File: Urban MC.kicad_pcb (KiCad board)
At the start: 4 copper layers, 166.4 x 125.1 mm, 78 parts, among them J1 Conn_01x02, J2 Conn_01x02, J3 Conn_01x03, J4 Conn_01x02, Q1 IQE022N06LM5CGSCATMA1, Q10 IQE022N06LM5CGSCATMA1, Q11 IQE022N06LM5CGSCATMA1, Q12 IQE022N06LM5CGSCATMA1, Q13 IQE022N06LM5CGSCATMA1, Q14 IQE022N06LM5CGSCATMA1, Q15 IQE022N06LM5CGSCATMA1, Q16 IQE022N06LM5CGSCATMA1, Q17 IQE022N06LM5CGSCATMA1, Q18 IQE022N06LM5CGSCATMA1, Q19 IQE022N06LM5CGSCATMA1, Q2 IQE022N06LM5CGSCATMA1, Q20 IQE022N06LM5CGSCATMA1, Q21 IQE022N06LM5CGSCATMA1, Q22 IQE022N06LM5CGSCATMA1, Q23 IQE022N06LM5CGSCATMA1, Q24 IQE022N06LM5CGSCATMA1, Q3 IQE022N06LM5CGSCATMA1, Q4 IQE022N06LM5CGSCATMA1, Q5 IQE022N06LM5CGSCATMA1, Q6 IQE022N06LM5CGSCATMA1, Q7 IQE022N06LM5CGSCATMA1, Q8 IQE022N06LM5CGSCATMA1, Q9 IQE022N06LM5CGSCATMA1, SW1 CAN_TERM, SW2 SW_Push, U1 MCP2561/2, U2 MCP4725, U3 MCP2515-xSO, Y1 8MHz

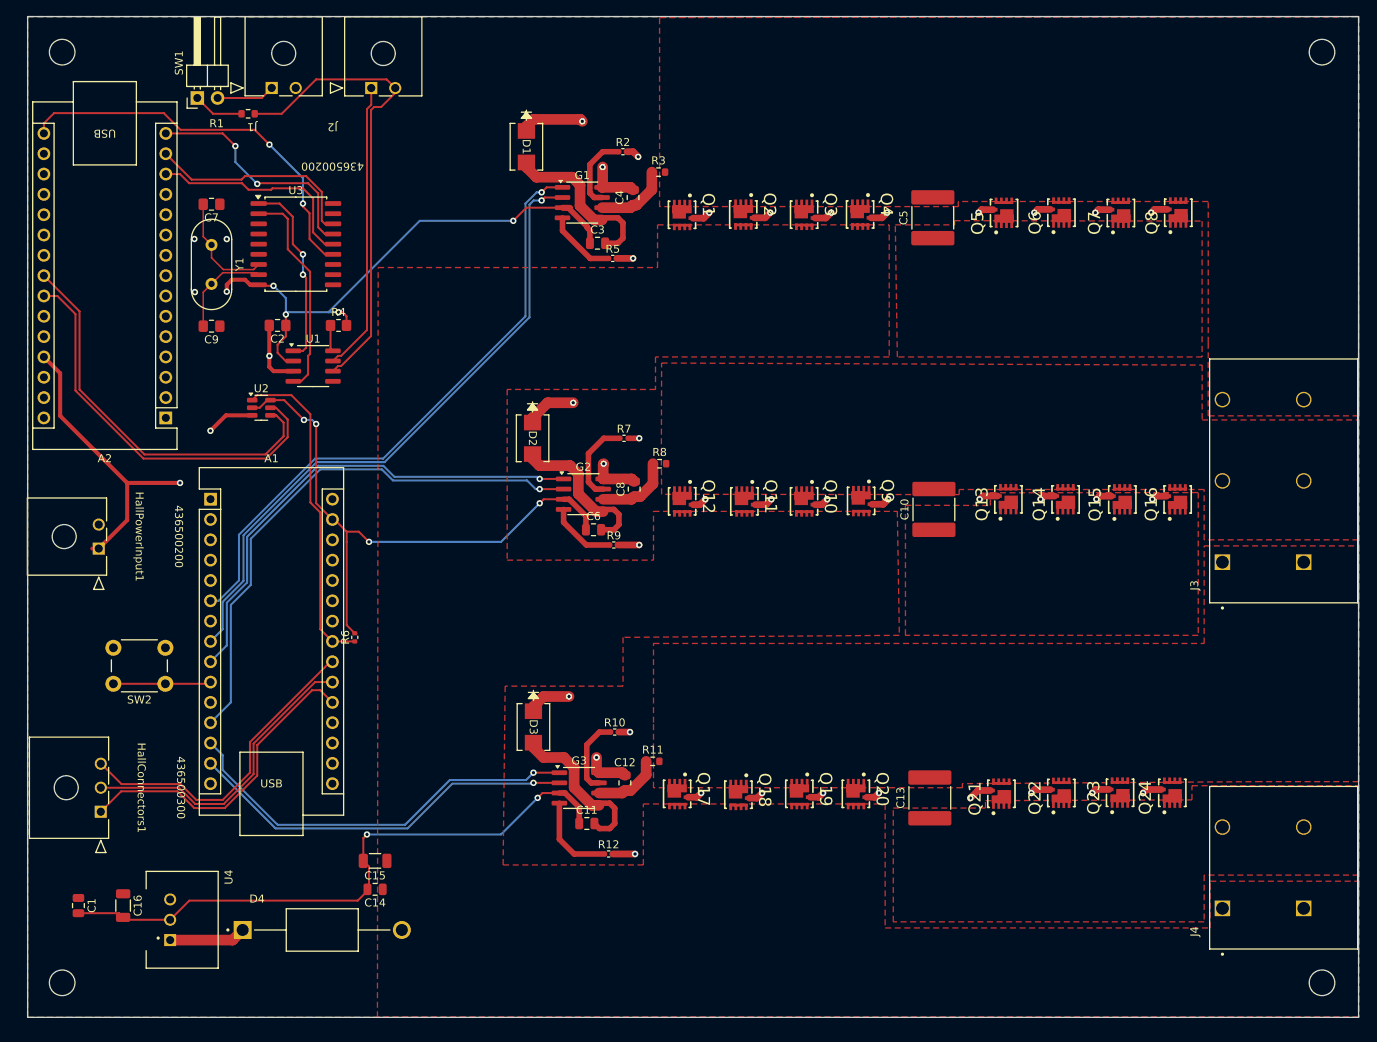
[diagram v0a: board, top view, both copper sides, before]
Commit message: Duplicated filled zones, finished CAN section, organized component labels
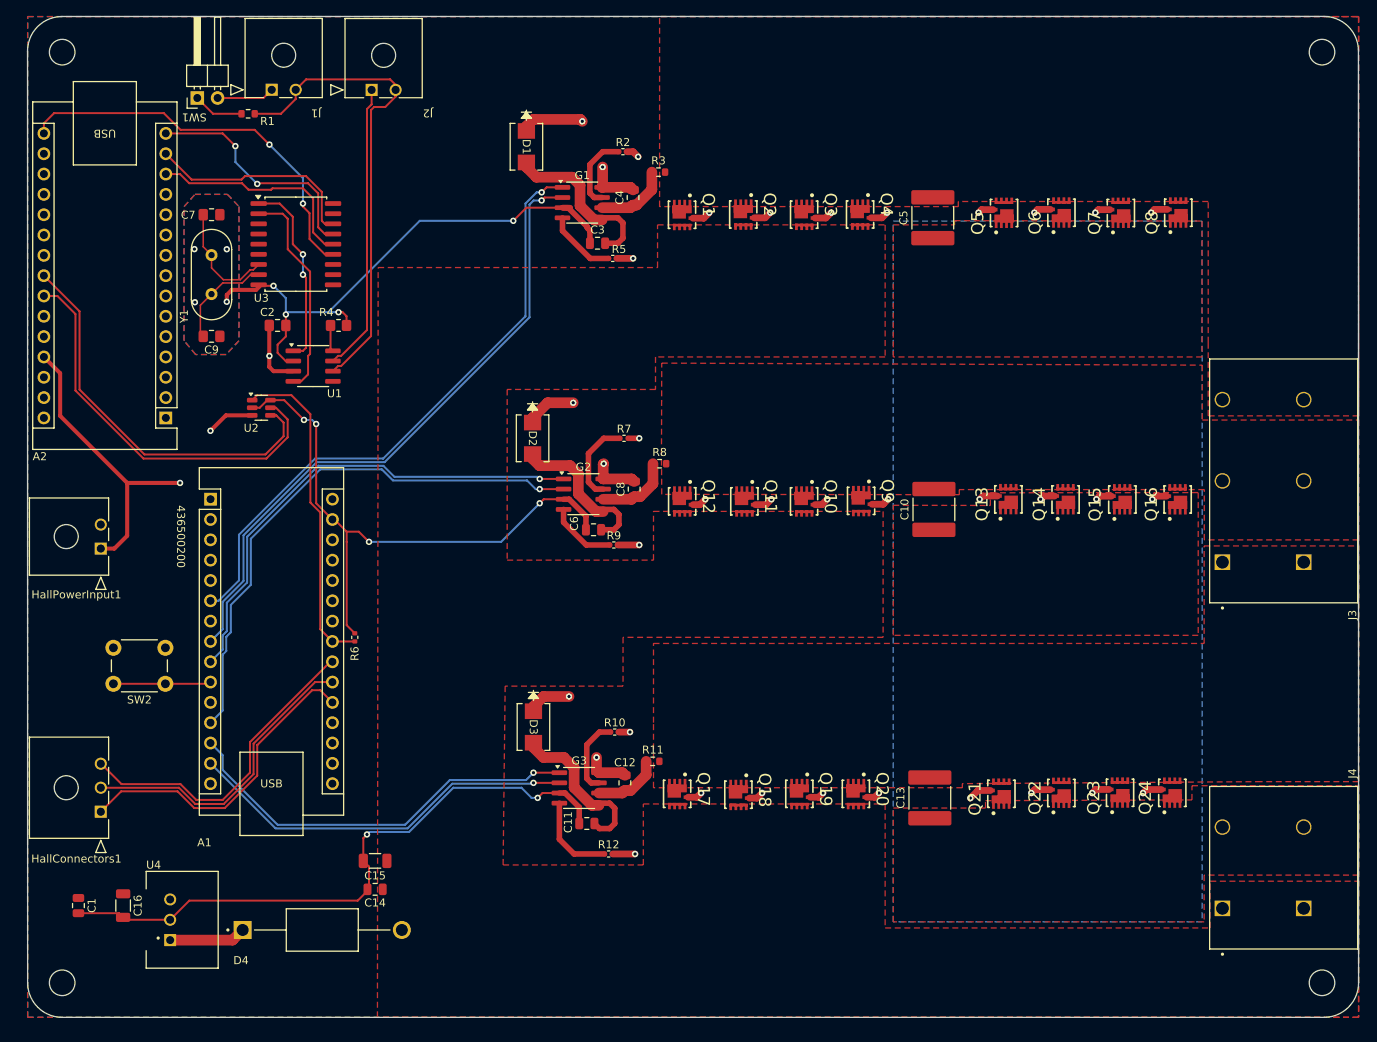
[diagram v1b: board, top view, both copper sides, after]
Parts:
- moved C7 1.31 mm to (115.7, 53.3)
- moved C9 1.27 mm to (115.7, 68.5)
- moved Y1 1.27 mm to (115.7, 58.4)
- moved HallPowerInput1 0.26 mm to (101.9, 95.1)
- moved J2 0.24 mm to (135.7, 37.7)
- moved J1 0.23 mm to (123.2, 37.7)
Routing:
- net /CAN LOW: track 59.2 -> 61.0 mm
- net GND: track 220.3 -> 221.5 mm
- net C-: track 12.3 -> 12.9 mm
- added copper zone on In1.Cu, net +48V
- added copper zone on B.Cu, net GND
- added copper zone on In1.Cu, net Net-(J3-Pin_1)
- added copper zone on In1.Cu, net Net-(J3-Pin_2)
- added copper zone on In1.Cu, net Net-(J3-Pin_3)
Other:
- outline, holes or cut-outs redrawn

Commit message: vias
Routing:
- net Net-(J3-Pin_3): vias 0 -> 61
- net Net-(J3-Pin_2): vias 0 -> 33
- net Net-(J3-Pin_1): vias 0 -> 41
- net GND: vias 14 -> 94
- net +48V: vias 0 -> 180

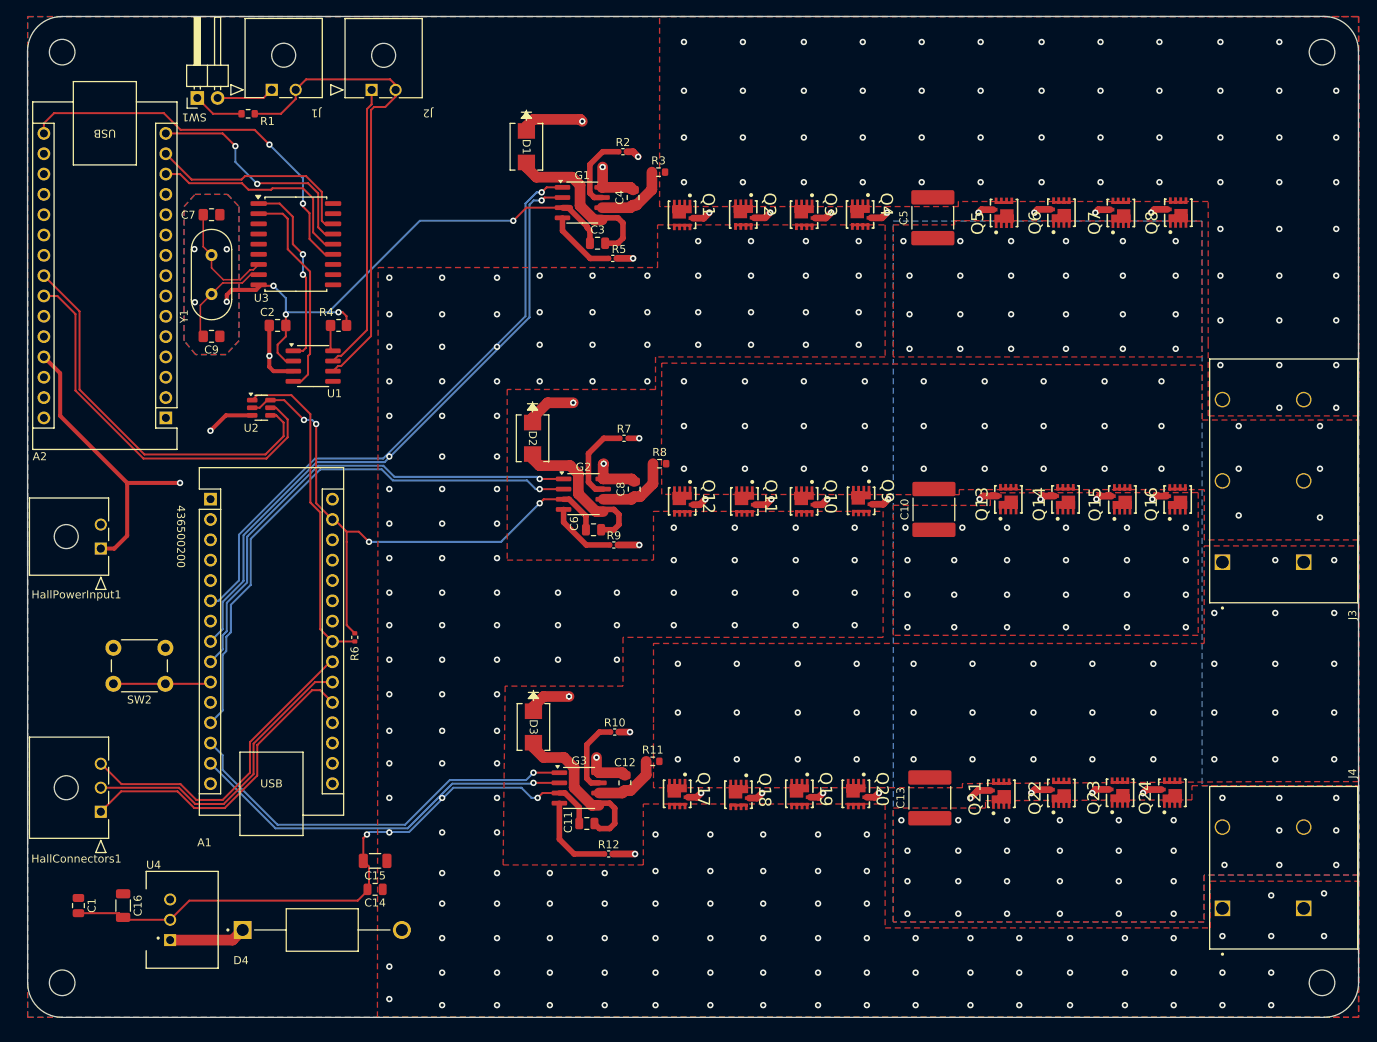
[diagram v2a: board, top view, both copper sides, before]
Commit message: connector labels
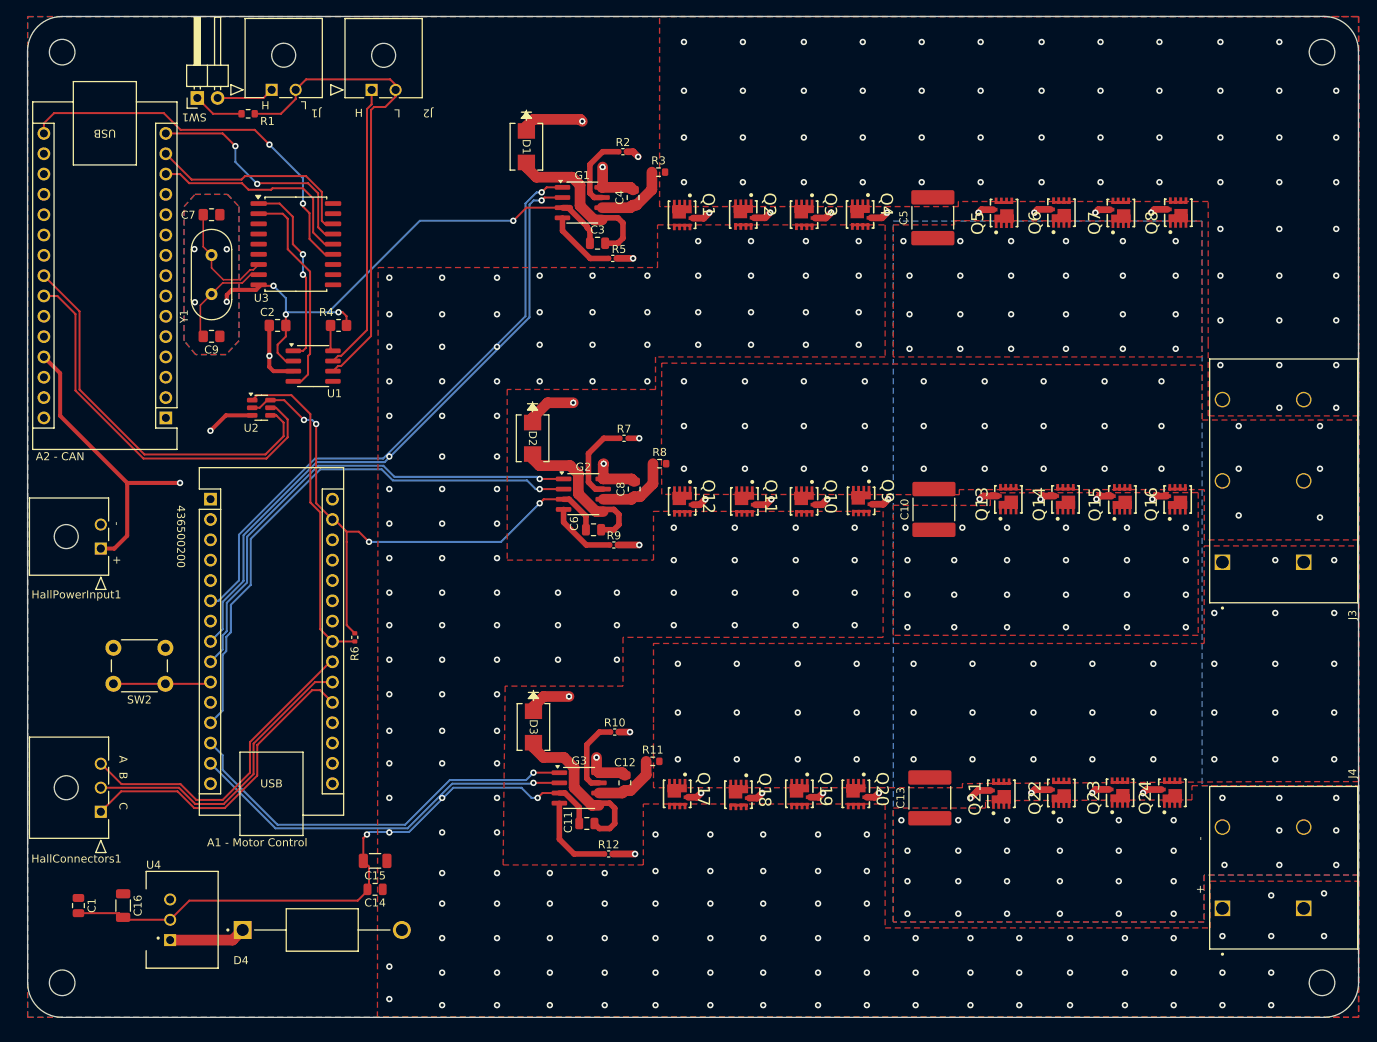
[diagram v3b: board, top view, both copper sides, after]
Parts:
- A1 - Motor Control: renamed from A1
- A2 - CAN: renamed from A2
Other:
- board text added: "+"
- board text added: "-"
- board text added: "A"
- board text added: "B"
- board text added: "C"
- board text added: "H"
- board text added: "L"
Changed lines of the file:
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@@
 		(descr "Arduino Nano, http://www.mouser.com/pdfdocs/Gravitech_Arduino_Nano3_0.pdf")
 		(tags "Arduino Nano")
-		(property "Reference" "A1"
-			(at -0.762 42.926 0)
+		(property "Reference" "A1 - Motor Control"
+			(at 5.842 42.926 0)
 			(layer "F.SilkS")
 			(effects
@@
 		(descr "Arduino Nano, http://www.mouser.com/pdfdocs/Gravitech_Arduino_Nano3_0.pdf")
 		(tags "Arduino Nano")
-		(property "Reference" "A2"
-			(at 15.748 -4.826 0)
+		(property "Reference" "A2 - CAN"
+			(at 13.208 -4.826 0)
 			(layer "F.SilkS")
 			(effects
@@
 			)
 		)
-		(fp_text user "${REFERENCE}"
-			(at 2.613506 -1.630764 180)
-			(unlocked yes)
-			(layer "F.Fab")
-			(effects
-				(font
-					(size 1 1)
-					(thickness 0.15)
-				)
-			)
-		)
 		(pad "" np_thru_hole circle
 			(at -1.5 4.319999 180)
@@
 		(layer "Edge.Cuts")
 	)
+	(gr_text "C\n"
+		(at 104.648 127.254 270)
+		(layer "F.SilkS")
+		(effects
+			(font
+				(size 1 1)
+				(thickness 0.15)
+			)
+		)
+	)
+	(gr_text "+\n"
+		(at 103.886 96.52 270)
+		(layer "F.SilkS")
+		(effects
+			(font
+				(size 1 1)
+				(thickness 0.15)
+			)
+		)
+	)
+	(gr_text "+"
+		(at 239.268 137.668 90)
+		(layer "F.SilkS")
+		(effects
+			(font
+				(size 1 1)
+				(thickness 0.15)
+			)
+		)
+	)
+	(gr_text "H\n"
+		(at 134.112 40.64 0)
+		(layer "F.SilkS")
+		(effects
+			(font
+				(size 1 1)
+				(thickness 0.15)
+			)
+		)
+	)
+	(gr_text "H\n"
+		(at 122.428 39.624 180)
+		(layer "F.SilkS")
+		(effects
+			(font
+				(size 1 1)
+				(thickness 0.15)
+			)
+		)
+	)
+	(gr_text "L"
+		(at 138.938 40.64 180)
+		(layer "F.SilkS")
+		(effects
+			(font
+				(size 1 1)
+				(thickness 0.15)
+			)
+		)
+	)
+	(gr_text "-\n"
+		(at 239.268 131.318 90)
+		(layer "F.SilkS")
+		(effects
+			(font
+				(size 1 1)
+				(thickness 0.15)
+			)
+		)
+	)
+	(gr_text "-"
+		(at 103.886 91.948 270)
+		(layer "F.SilkS")
+		(effects
+			(font
+				(size 1 1)
+				(thickness 0.15)
+			)
+		)
+	)
+	(gr_text "L\n"
+		(at 127.254 39.624 180)
+		(layer "F.SilkS")
+		(effects
+			(font
+				(size 1 1)
+				(thickness 0.15)
+			)
+		)
+	)
+	(gr_text "A"
+		(at 104.648 121.412 -90)
+		(layer "F.SilkS")
+		(effects
+			(font
+				(size 1 1)
+				(thickness 0.15)
+			)
+		)
+	)
+	(gr_text "B\n"
+		(at 104.648 123.444 270)
+		(layer "F.SilkS")
+		(effects
+			(font
+				(size 1 1)
+				(thickness 0.15)
+			)
+		)
+	)
 	(segment

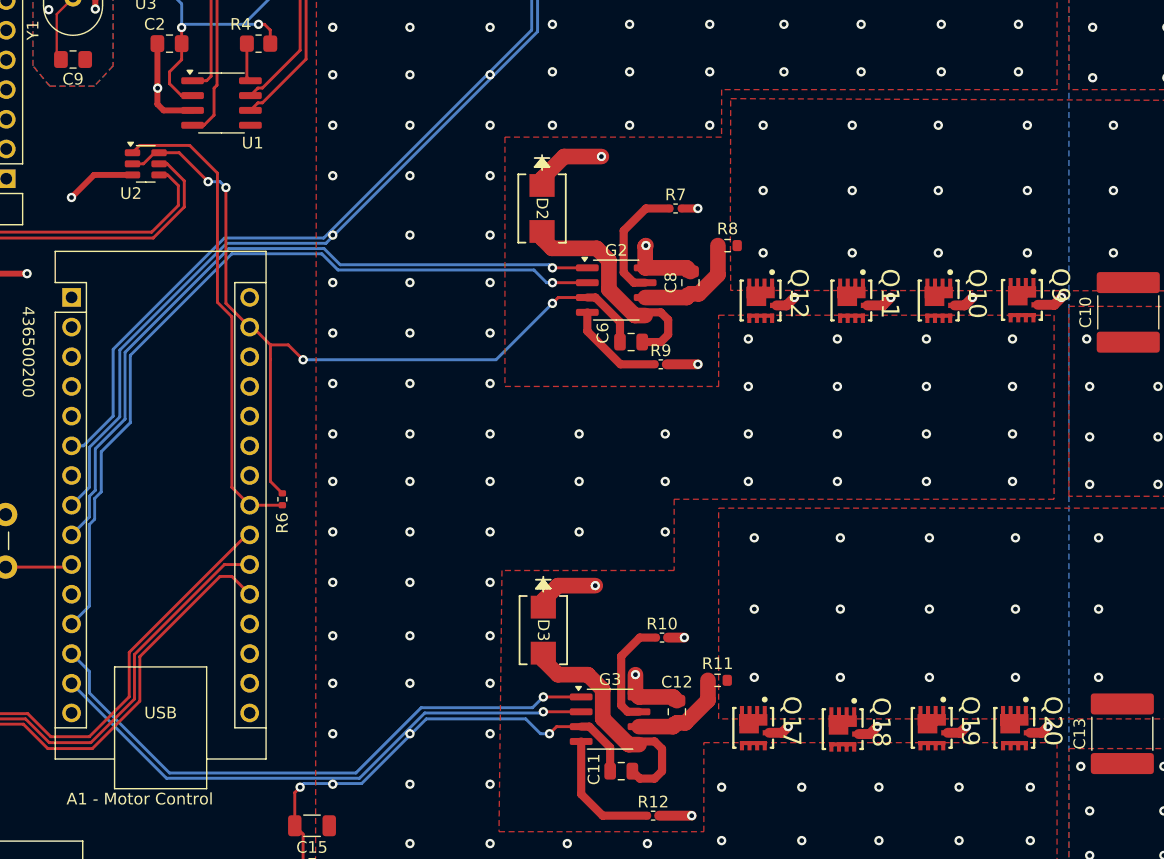
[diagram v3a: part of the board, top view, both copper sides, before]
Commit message: final edits: power 12V islands, adjusting vias to pass DRC
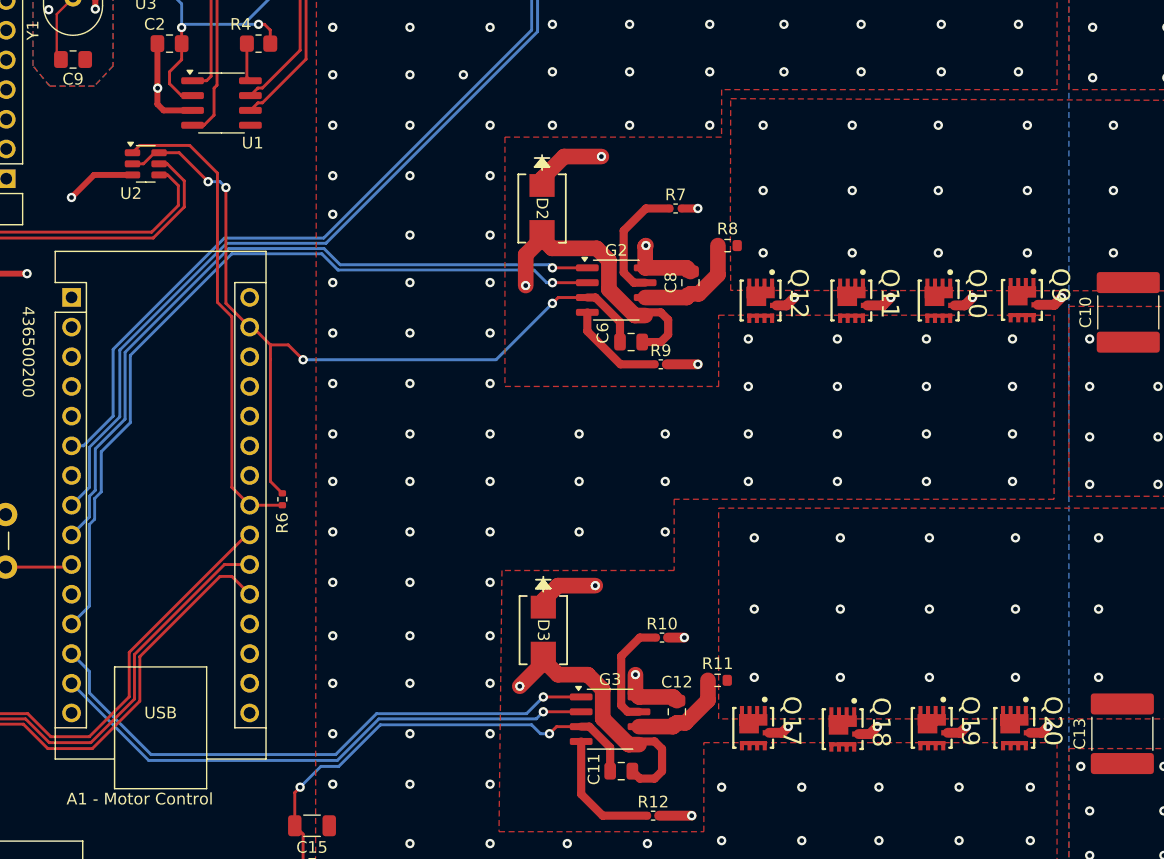
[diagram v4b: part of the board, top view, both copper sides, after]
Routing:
- net +12V: track 61.6 -> 140.8 mm, vias 0 -> 2
- net Net-(A1-D10): track 51.6 -> 50.3 mm
- net Net-(A1-D11): track 49.3 -> 48.1 mm
